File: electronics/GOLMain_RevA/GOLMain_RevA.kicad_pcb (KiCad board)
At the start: 2 copper layers, 70 x 70 mm, 53 parts, among them P1 CONN_ID_0, P10 CONN_ID_6, P11 CONN_ID_7, P12 CONN_LED, P13 CONN_FTDI, P14 CONN_V50SEL, P2 CONN_ID_1, P3 CONN_READERS, P4 CONN_ID_2, P5 CONN_MAIN1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

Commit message: near final version of pcb layout
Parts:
- added C7: 0.1uF, Capacitors_SMD:C_0805, F.Cu at (148.5, 127.0)
- added P15: CONN_AB_RES, Pin_Headers:Pin_Header_Straight_1x02, F.Cu at (114.0, 153.0)
- added P16: CONN_V12V50, Pin_Headers:Pin_Header_Straight_1x02, F.Cu at (123.8, 152.0)
- added P17: CONN_LEDCLK, Pin_Headers:Pin_Header_Straight_1x02, F.Cu at (150.0, 107.0)
- added P18: CONN_LEDDATA, Pin_Headers:Pin_Header_Straight_1x02, F.Cu at (141.0, 110.0)
- added P19: CONN_TX3350, Pin_Headers:Pin_Header_Straight_1x02, F.Cu at (122.0, 102.0)
- added P20: CONN_EN3350, Pin_Headers:Pin_Header_Straight_1x02, F.Cu at (111.0, 104.0)
- added P21: CONN_RX3350, Pin_Headers:Pin_Header_Straight_1x02, F.Cu at (100.0, 106.0)
- added R1: 470, Resistors_SMD:R_1206, F.Cu at (134.0, 110.0)
- added R2: 470, Resistors_SMD:R_1206, F.Cu at (143.0, 107.0)
- added R3: 100, Resistors_SMD:R_1206, F.Cu at (115.0, 150.0)
- added REF**: MountingHole_3mm, Mounting_Holes:MountingHole_3mm, F.Cu at (158.0, 158.0)
- added REF**: MountingHole_3mm, Mounting_Holes:MountingHole_3mm, F.Cu at (96.0, 158.0)
- added REF**: MountingHole_3mm, Mounting_Holes:MountingHole_3mm, F.Cu at (96.0, 96.0)
- added REF**: MountingHole_3mm, Mounting_Holes:MountingHole_3mm, F.Cu at (158.0, 96.0)
- C3, C4, P5, P6, SW1, SW2, U5, U6: moved to B.Cu
- P3: footprint Pin_Headers:Pin_Header_Straight_2x03 -> Sockets_MOLEX_KK-System:Socket_MOLEX-KK-RM2-54mm_Lock_4pin_straight
- moved R26 67.0 mm to (141.2, 139.5), turned to 180 degrees
- moved U6 66.7 mm to (134.5, 147.0), turned to 180 degrees
- moved P14 65.4 mm to (140.0, 145.5), turned to 180 degrees
- moved R25 60.6 mm to (136.2, 139.5), turned to 180 degrees
- moved C6 55.9 mm to (136.0, 143.5)
- moved RP2 46.1 mm to (98.0, 142.0), turned to 90 degrees
- moved P3 44.4 mm to (118.5, 127.0), turned to 270 degrees
- moved C5 42.9 mm to (117.0, 146.5), turned to 180 degrees
- moved P1 39.2 mm to (94.5, 125.5), turned to 270 degrees
- moved U3 38.0 mm to (98.0, 136.0), turned to 90 degrees
- moved P12 37.6 mm to (129.0, 134.5), turned to 90 degrees
- moved P2 36.3 mm to (94.5, 128.5), turned to 270 degrees
- moved P13 36.2 mm to (153.0, 104.0), turned to 90 degrees
- moved Q2 35.5 mm to (140.0, 114.0), turned to 90 degrees
- moved R16 34.1 mm to (137.0, 114.0)
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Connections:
- P12 pad 2: LED_DATA -> Net-(P12-Pad2)
- P12 pad 3: LED_CLOCK -> Net-(P12-Pad3)
- P3 pad 1: V33 -> GND
- P3 pad 2: V33 -> READER1
- P3 pad 3: GND -> READER2
- P3 pad 4: GND -> V33
- Q1 pad 2: SCL -> LED_CLOCK
- Q2 pad 2: SDA -> LED_DATA
- R13 pad 1: SCL -> LED_CLOCK
- R14 pad 1: SDA -> LED_DATA
- U2 pad 19: SDA -> LED_DATA
- U2 pad 20: SCL -> LED_CLOCK
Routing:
- net GND: track 0.00 -> 333.5 mm, vias 0 -> 7
- net V33: track 0.00 -> 260.7 mm, vias 0 -> 11
- net V50: track 0.00 -> 143.2 mm, vias 0 -> 7
- net RX33: track 0.00 -> 141.7 mm, vias 0 -> 4
- net V12: track 0.00 -> 138.6 mm
- net TX33: track 0.00 -> 130.9 mm, vias 0 -> 2
- net GPIO0: track 0.00 -> 108.8 mm, vias 0 -> 6
- net A: track 0.00 -> 103.7 mm, vias 0 -> 2
- net GPIO2: track 0.00 -> 101.9 mm, vias 0 -> 7
- net EN_MAX: track 0.00 -> 100.6 mm, vias 0 -> 3
- net B: track 0.00 -> 99.5 mm
- net ID_DATA: track 0.00 -> 49.6 mm, vias 0 -> 1
- net READER2: track 0.00 -> 34.7 mm, vias 0 -> 2
- net READER1: track 0.00 -> 34.3 mm, vias 0 -> 2
- net LED_CLOCK: track 0.00 -> 32.9 mm, vias 0 -> 1
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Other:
- outline, holes or cut-outs redrawn
- board text added: "--V33 --ID --GND"
- board text added: "2^0= 1 2^1= 2 2^2= 4 2^3= 8 2^4= 16 2^5= 32 2^6= 64 2^7=128"
- board text added: "Poor man's 5V"
- board text removed: "2^0 = 1 2^1 = 2 2^2 = 4 2^3 = 8 2^4 = 16 2^5 = 32 2^6 = 64 2^7 = 128"

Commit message: updated main pcb to final version
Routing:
- net V12: track 138.6 -> 171.0 mm, vias 0 -> 2
- net GND: track 333.5 -> 344.8 mm, vias 7 -> 6
- net ID_4: track 24.9 -> 33.6 mm, vias 3 -> 1
- net V33: track 260.7 -> 253.4 mm
- net GPIO0: track 108.8 -> 115.9 mm, vias 6 -> 8
- net GPIO2: track 101.9 -> 104.7 mm, vias 7 -> 9
- net RX50: track 19.1 -> 17.3 mm
- net A: track 103.7 -> 102.0 mm
- net V50: track 143.2 -> 142.1 mm
- net RX33: track 141.7 -> 142.8 mm
- net ID_DATA: vias 1 -> 3
- net EN_MAX: vias 3 -> 5
- added copper zone on B.Cu, net GND
- added copper zone on F.Cu, net V12
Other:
- board text added: "GND A B V12"
- board text added: "GND R1 R2 V33"
- board text added: "GOLMain RevA Matthew Swarts 2017.03.17"
- board text added: "RX3 EN3 EN3 TX3"
- board text added: "RX5 EN5 EN5 TX5"
- board text added: "SW_PROG"
- board text added: "SW_RESET"
- board text added: "V12 CLK DAT GND"
- board text added: "V33 B A GND"
- board text added: "V50 B A GND"

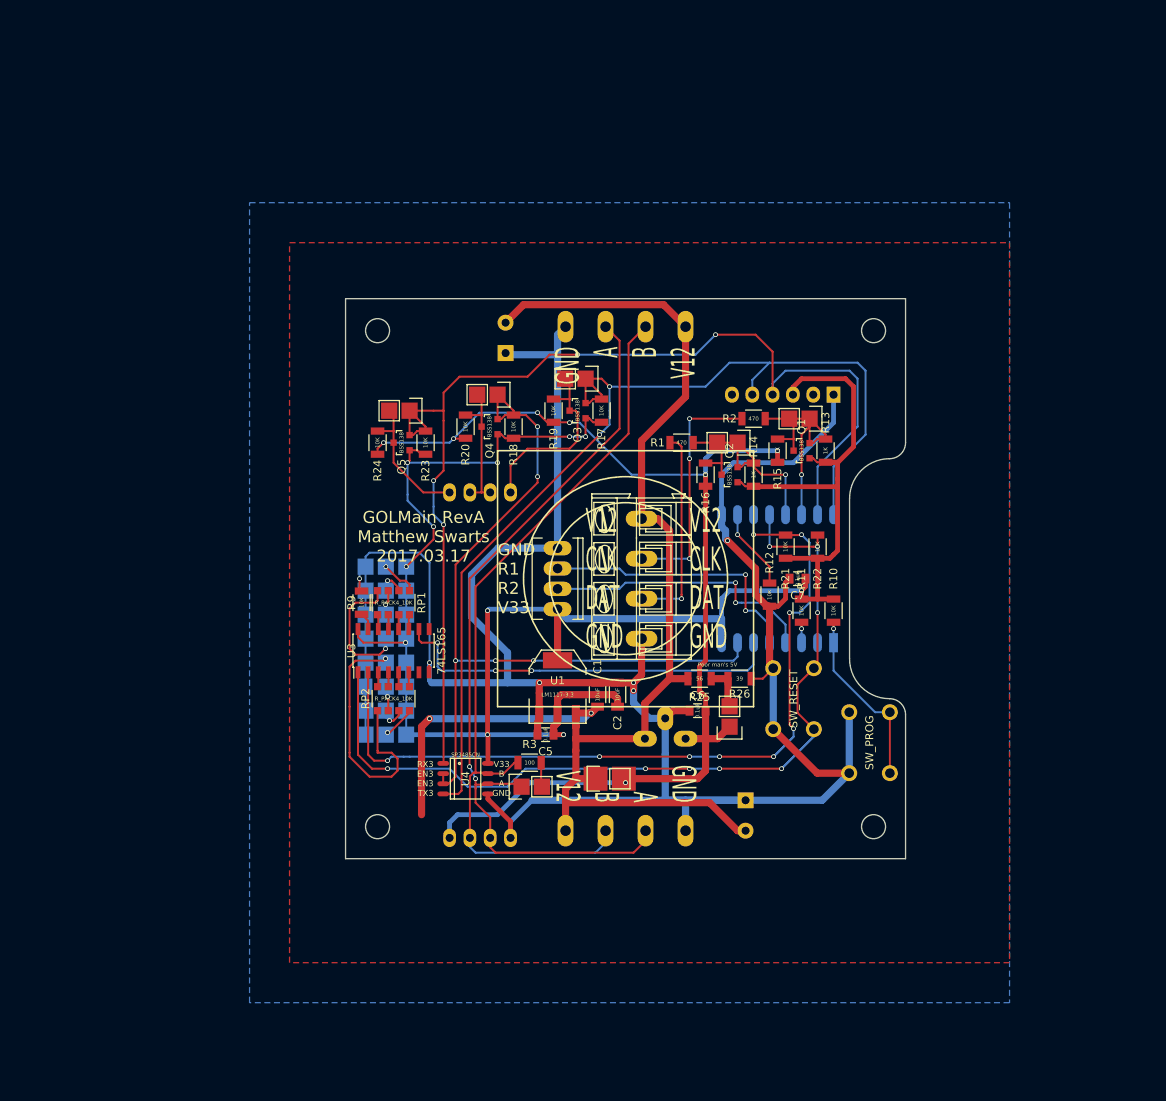
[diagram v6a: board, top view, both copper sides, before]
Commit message: refined main board, shift 4 pin led conn, made more space for gnd and v12 planes; created tcrt5000 module
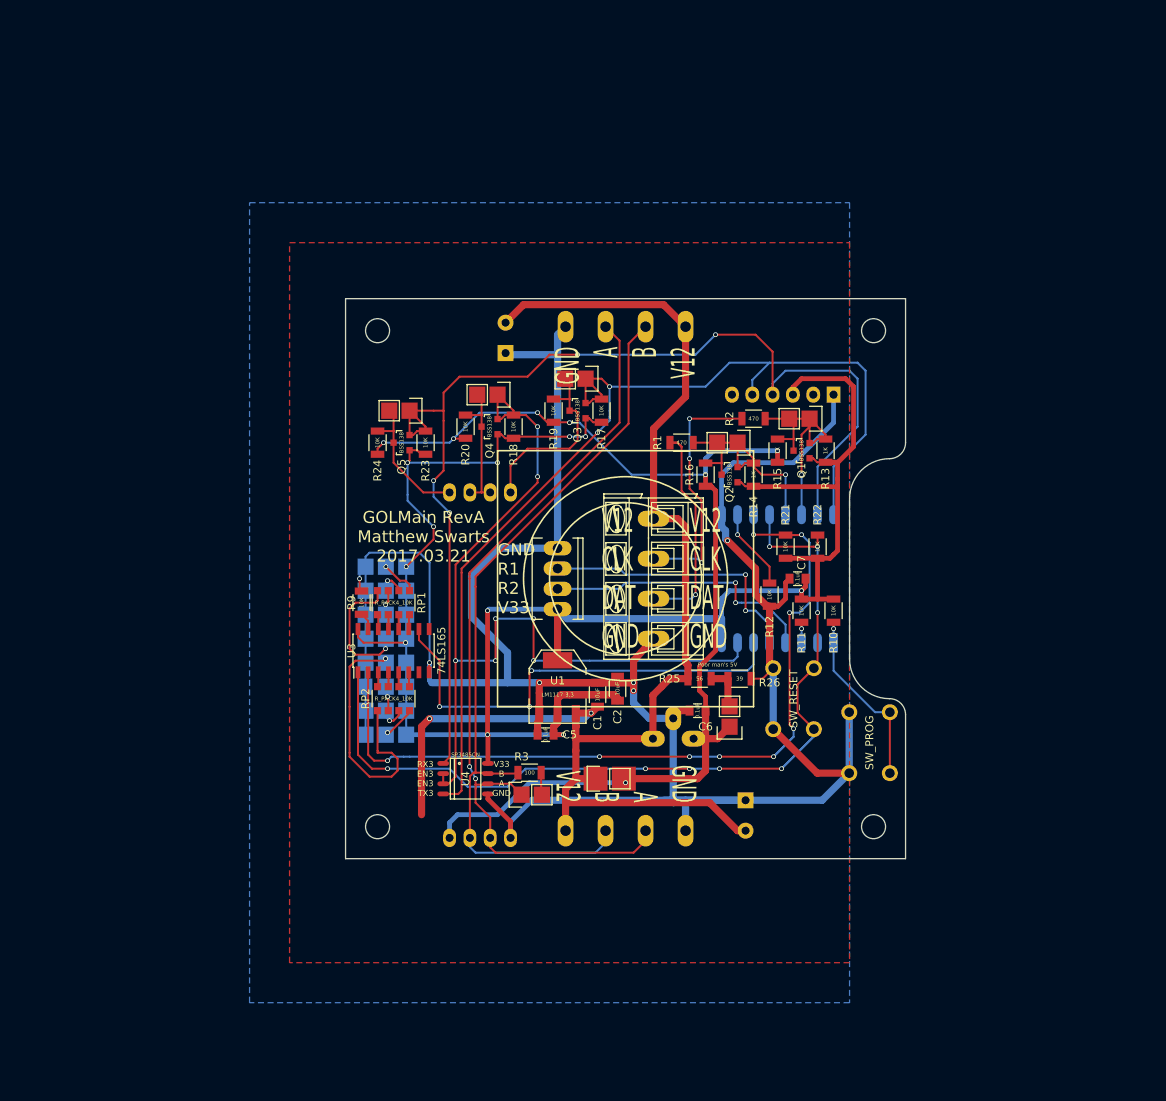
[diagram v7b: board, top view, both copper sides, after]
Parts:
- moved P12 1.50 mm to (130.5, 134.5)
- moved R3 1.25 mm to (115.0, 151.2)
- moved P15 1.00 mm to (114.0, 154.0)
- moved U6 1.00 mm to (135.5, 147.0)
- moved C2 0.75 mm to (126.0, 140.8)
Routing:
- net EN_MAX: track 100.6 -> 111.1 mm, vias 5 -> 7
- net GND: track 344.8 -> 354.6 mm
- net ID_DATA: track 49.6 -> 57.4 mm
- net V33: track 253.4 -> 259.8 mm
- net Net-(P12-Pad2): track 25.7 -> 28.0 mm
- net Net-(P12-Pad3): track 30.1 -> 31.4 mm
- net A: track 102.0 -> 103.0 mm
- net V12: track 171.0 -> 171.9 mm
- net RX33: track 142.8 -> 143.5 mm
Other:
- board text added: "GOLMain RevA Matthew Swarts 2017.03.21"
- board text removed: "GOLMain RevA Matthew Swarts 2017.03.17"

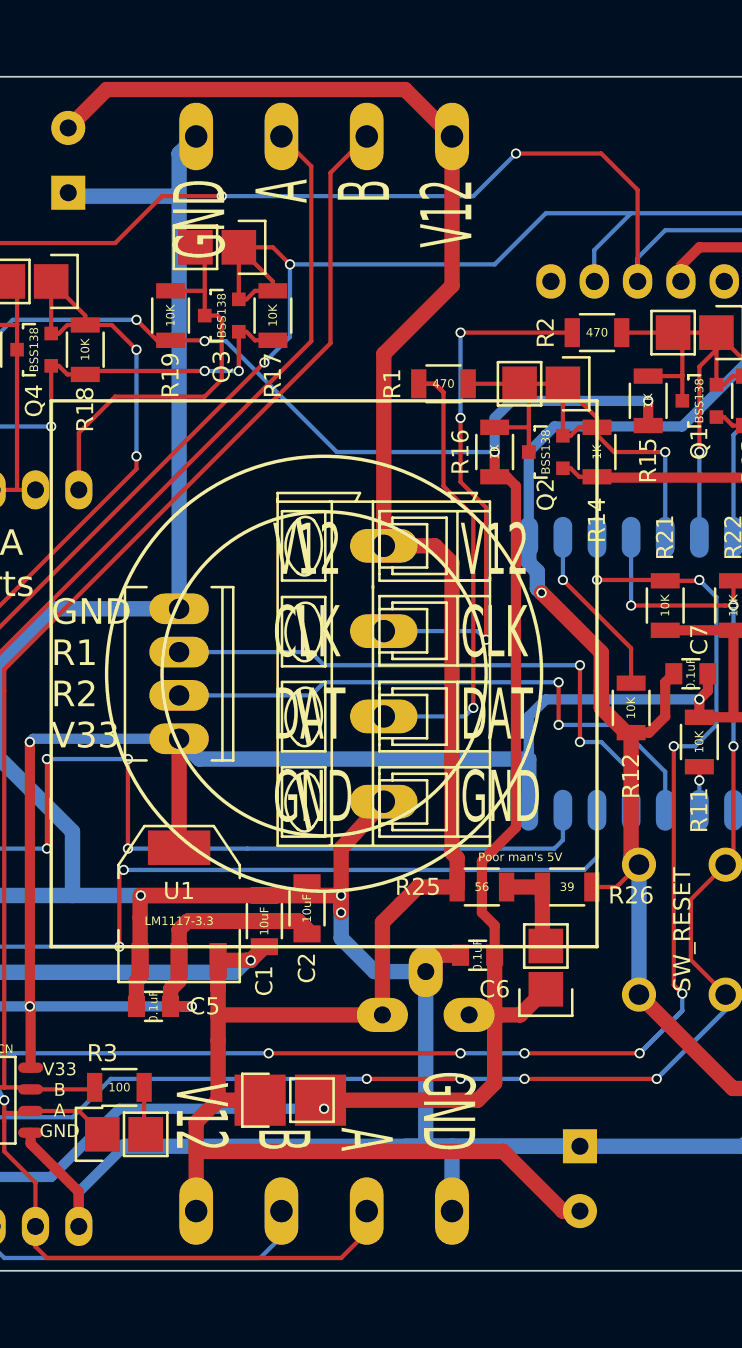
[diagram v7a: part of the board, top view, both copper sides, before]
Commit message: added basic station string test firmware
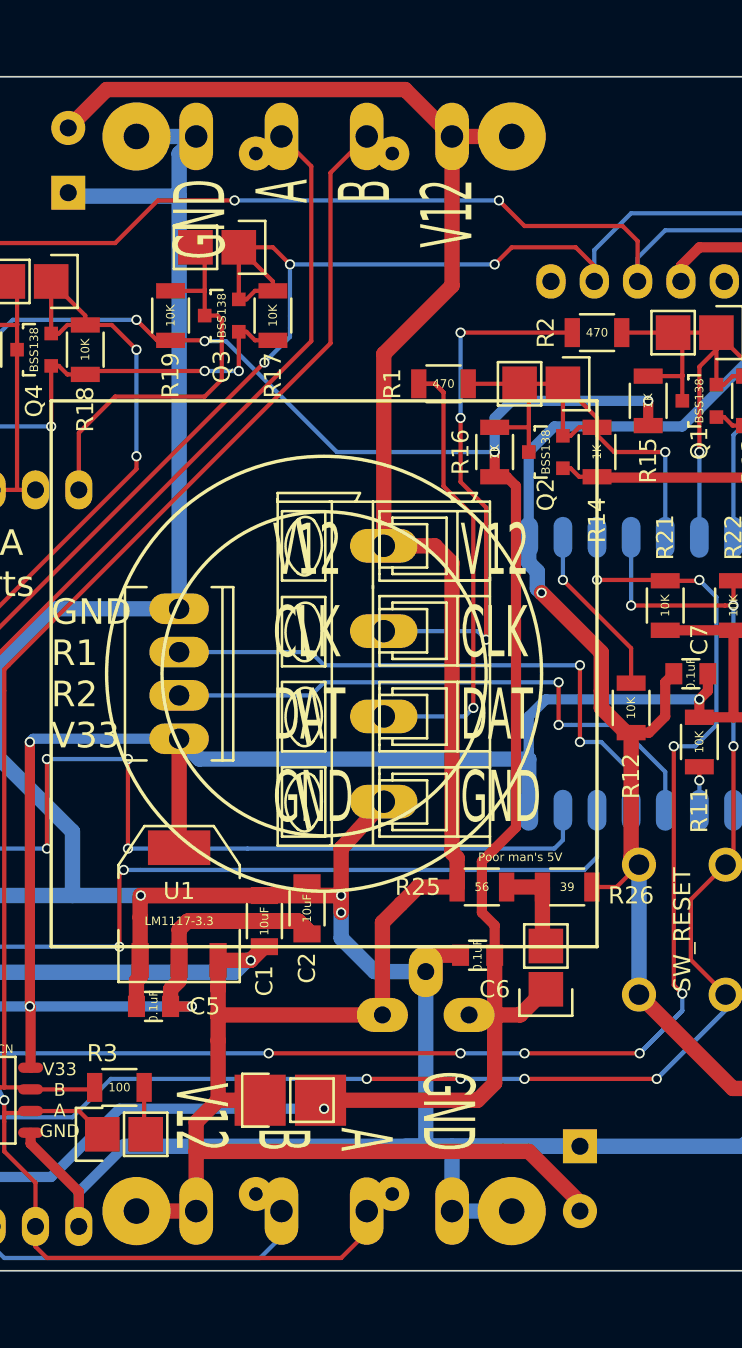
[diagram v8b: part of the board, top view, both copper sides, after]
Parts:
- added P22: CONN_GND, Wire_Pads:SolderWirePad_single_1-5mmDrill, F.Cu at (138.0, 158.5)
- added P23: CONN_A, Wire_Pads:SolderWirePad_single_0-8mmDrill, F.Cu at (131.0, 157.5)
- added P24: CONN_B, Wire_Pads:SolderWirePad_single_0-8mmDrill, F.Cu at (123.0, 157.5)
- added P25: CONN_V12, Wire_Pads:SolderWirePad_single_1-5mmDrill, F.Cu at (116.0, 158.5)
- added P26: CONN_GND, Wire_Pads:SolderWirePad_single_1-5mmDrill, F.Cu at (116.0, 95.5)
- added P27: CONN_A, Wire_Pads:SolderWirePad_single_0-8mmDrill, F.Cu at (123.0, 96.5)
- added P28: CONN_B, Wire_Pads:SolderWirePad_single_0-8mmDrill, F.Cu at (131.0, 96.5)
- added P29: CONN_V12, Wire_Pads:SolderWirePad_single_1-5mmDrill, F.Cu at (138.0, 95.5)
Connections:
- P13 pad 2: CTS -> (no net)
- P13 pad 6: RTS -> (no net)
- U2 pad 2: Net-(U2-Pad2) -> (no net)
- U3 pad 7: Net-(U3-Pad7) -> (no net)
- U3 pad 9: Net-(U3-Pad9) -> (no net)
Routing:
- net V12: track 171.9 -> 179.2 mm
- net GND: track 354.6 -> 361.6 mm
- net RX33: track 143.5 -> 139.5 mm
- net A: track 103.0 -> 106.8 mm
- net B: track 99.1 -> 102.9 mm
- net TX33: track 130.9 -> 129.3 mm, vias 2 -> 3
